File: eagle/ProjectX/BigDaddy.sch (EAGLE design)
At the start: 180 parts, among them T1 MA40S4S, T10 MA40S4S, T11 MA40S4S, T12 MA40S4S, T13 MA40S4S, T14 MA40S4S, T15 MA40S4S, T16 MA40S4S, T17 MA40S4S, T18 MA40S4S, T19 MA40S4S, T2 MA40S4S, T20 MA40S4S, T21 MA40S4S, T22 MA40S4S, T23 MA40S4S, T24 MA40S4S, T25 MA40S4S, T26 MA40S4S, T27 MA40S4S, T28 MA40S4S, T3 MA40S4S, T30 MA40S4S, T31 MA40S4S, T32 MA40S4S, T33 MA40S4S, T34 MA40S4S, T35 MA40S4S, T36 MA40S4S, T37 MA40S4S, T38 MA40S4S, T39 MA40S4S, T4 MA40S4S, T40 MA40S4S, T41 MA40S4S, T42 MA40S4S, T43 MA40S4S, T44 MA40S4S, T45 MA40S4S, T46 MA40S4S, T47 MA40S4S, T48 MA40S4S, T49 MA40S4S, T5 MA40S4S, T50 MA40S4S, T51 MA40S4S, T52 MA40S4S, T53 MA40S4S, T54 MA40S4S, T55 MA40S4S, T56 MA40S4S, T57 MA40S4S, T58 MA40S4S, T59 MA40S4S, T6 MA40S4S, T60 MA40S4S, T61 MA40S4S, T62 MA40S4S, T63 MA40S4S, T64 MA40S4S, T65 MA40S4S, T66 MA40S4S, T67 MA40S4S, T68 MA40S4S, T69 MA40S4S, T7 MA40S4S, T70 MA40S4S, T71 MA40S4S, T72 MA40S4S, T73 MA40S4S, T74 MA40S4S, T75 MA40S4S, T76 MA40S4S, T77 MA40S4S, T78 MA40S4S, T79 MA40S4S, T8 MA40S4S, T80 MA40S4S, T81 MA40S4S, T82 MA40S4S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

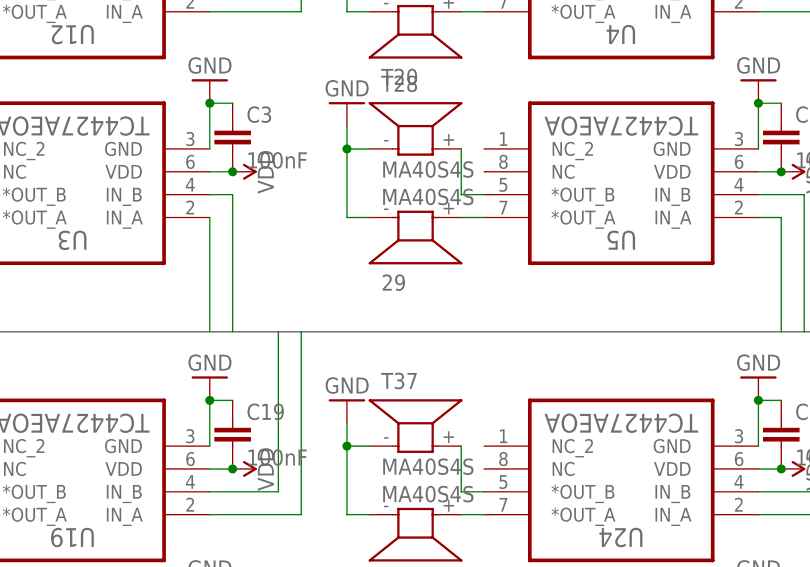
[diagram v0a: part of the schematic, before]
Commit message: Numbering T29
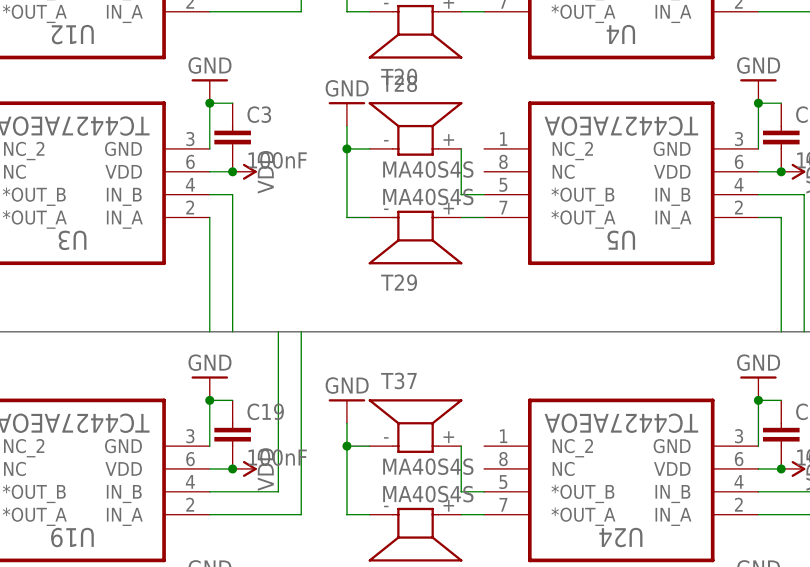
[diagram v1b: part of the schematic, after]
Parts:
- renumbered 29 to T29
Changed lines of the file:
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@@
 <part name="SUPPLY6" library="SparkFun-PowerSymbols" library_urn="urn:adsk.eagle:library:530" deviceset="VDD" device=""/>
 <part name="C4" library="resistor" library_urn="urn:adsk.eagle:library:348" deviceset="C-EU" device="C0805" package3d_urn="urn:adsk.eagle:package:26137/1" value="100nF"/>
-<part name="29" library="Parts" deviceset="MA40S4S" device=""/>
+<part name="T29" library="Parts" deviceset="MA40S4S" device=""/>
 <part name="T28" library="Parts" deviceset="MA40S4S" device=""/>
 <part name="U5" library="Parts" deviceset="TC4427AEOA" device=""/>
@@
 <instance part="SUPPLY6" gate="VDD" x="-43.18" y="-10.16" rot="R270"/>
 <instance part="C4" gate="G$1" x="-43.18" y="-5.08"/>
-<instance part="29" gate="G$1" x="-83.82" y="-38.1" rot="MR180"/>
+<instance part="T29" gate="G$1" x="-83.82" y="-38.1" rot="MR180"/>
 <instance part="T28" gate="G$1" x="-83.82" y="-30.48"/>
 <instance part="U5" gate="A" x="-63.5" y="-38.1" rot="R180"/>
@@
 </segment>
 <segment>
-<pinref part="29" gate="G$1" pin="1"/>
+<pinref part="T29" gate="G$1" pin="1"/>
 <wire x1="-88.9" y1="-38.1" x2="-91.44" y2="-38.1" width="0.1524" layer="91"/>
 <wire x1="-91.44" y1="-38.1" x2="-91.44" y2="-30.48" width="0.1524" layer="91"/>
@@
 <segment>
 <pinref part="U5" gate="A" pin="*OUT_A"/>
-<pinref part="29" gate="G$1" pin="2"/>
+<pinref part="T29" gate="G$1" pin="2"/>
 <wire x1="-76.2" y1="-38.1" x2="-78.74" y2="-38.1" width="0.1524" layer="91"/>
 </segment>
